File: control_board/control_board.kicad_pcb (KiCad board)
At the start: 2 copper layers, 51.2 x 76.2 mm, 43 parts, among them J1 Conn_01x08_Male, K1 G5Q-1A, Q1 Q_NPN_BEC, U1 MC78M05_TO252, U2 TSR_1-24120, U3 74LS02, U4 74LS02, U5 Conn_01x08_Male

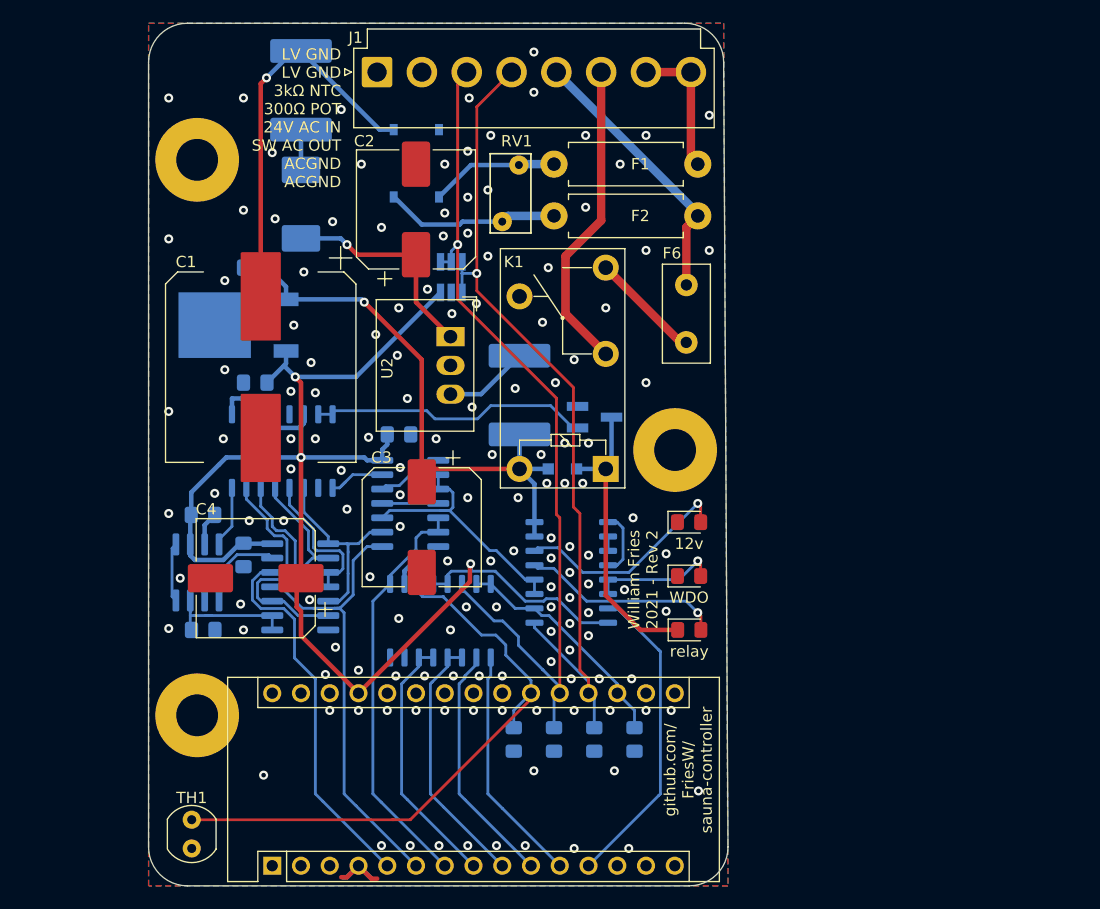
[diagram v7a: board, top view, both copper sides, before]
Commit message: Fix right edge cut
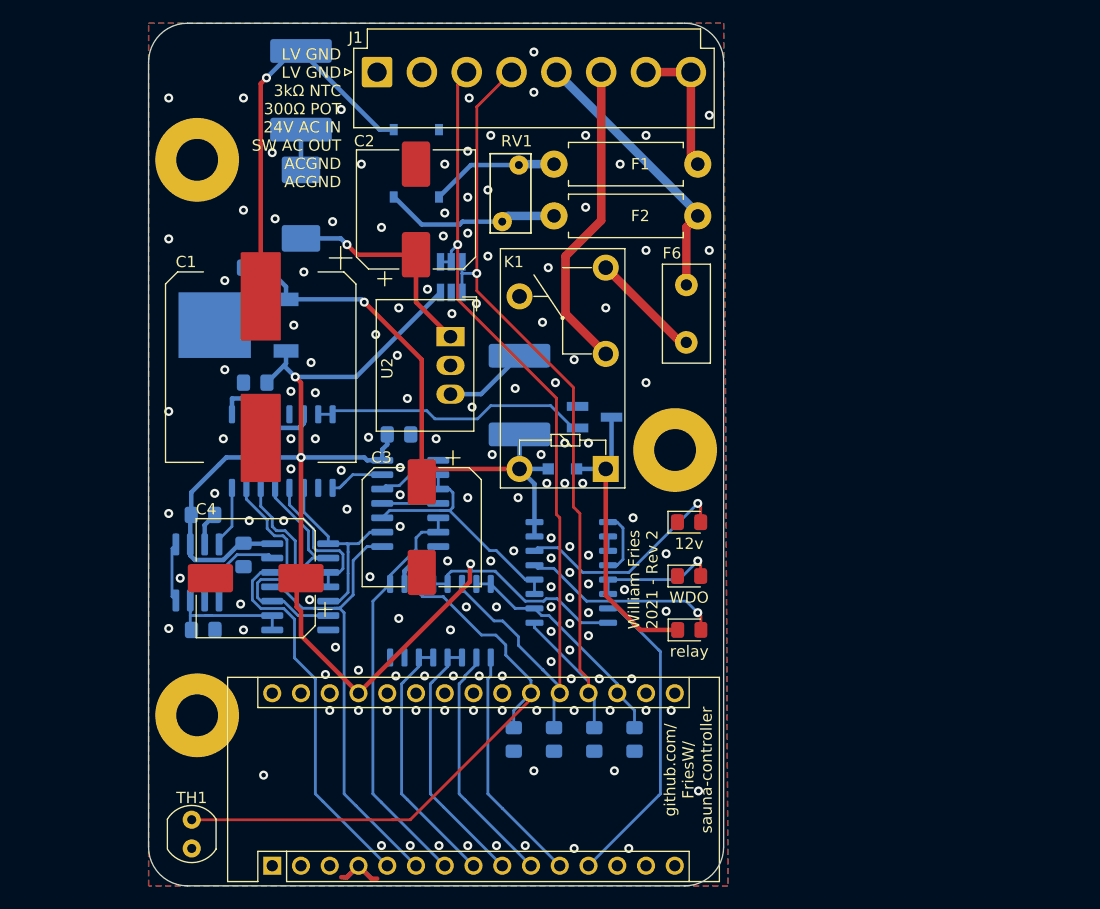
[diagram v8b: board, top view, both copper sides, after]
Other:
- board size 51.2 x 76.2 mm -> 50.8 x 76.2 mm
